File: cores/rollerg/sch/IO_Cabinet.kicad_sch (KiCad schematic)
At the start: 0 parts

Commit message: wip rollerg sch: SOUND
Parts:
- added C19, C20, C21, C23: 74LS253, symbol 74xx:74LS253
- added F14: 74LS04, symbol jt74:74LS04
- added RN1, RN2, RN3, RN4, RN5: KONAMI_005273, symbol konami:KONAMI_005273
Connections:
- new net: C23.3 (I3a), RN5.1 (YO)
- new net: C23.4 (I2a), RN5.3 (Y1)
- new net: C23.13 (I3b), RN5.5 (Y2)
- new net: C23.12 (I2b), RN5.7 (Y3)
- new net: C19.5 (I1a), RN2.1 (YO)
- new net: C19.11 (I1b), RN2.3 (Y1)
- new net: C20.5 (I1a), RN2.5 (Y2)
- new net: C20.11 (I1b), RN2.7 (Y3)
- new net: C20.3 (I3a), RN3.1 (YO)
- new net: C20.4 (I2a), RN3.3 (Y1)
- new net: C20.13 (I3b), RN3.5 (Y2)
- new net: C20.12 (I2b), RN3.7 (Y3)
- new net: C19.12 (I2b), RN1.7 (Y3)
- new net: C19.13 (I3b), RN1.5 (Y2)
- new net: C19.3 (I3a), RN1.1 (YO)
- new net: C19.4 (I2a), RN1.3 (Y1)
- new net: C21.3 (I3a), RN4.1 (YO)
- new net: C21.4 (I2a), RN4.3 (Y1)
- new net: C21.13 (I3b), RN4.5 (Y2)
- new net: C21.12 (I2b), RN4.7 (Y3)
- new net DB0: C21.9 (Zb)
- new net DB1: C21.7 (Za)
- new net DB2: C23.9 (Zb)
- new net DB3: C23.7 (Za)
- new net DB4: C20.9 (Zb)
- new net DB5: C20.7 (Za)
- new net DB6: C19.9 (Zb)
- new net DB7: C19.7 (Za)
- new net MAIN_A1: F14.1
- new net MOE: C19.1 (OEa), C19.15 (OEb), C20.1 (OEa), C20.15 (OEb), C21.1 (OEa), C21.15 (OEb), C23.1 (OEa), C23.15 (OEb)
- new net SMU: C19.14 (A0), C20.14 (A0), C21.14 (A0), C23.14 (A0)
- new net SMUB: C19.2 (A1), C20.2 (A1), C21.2 (A1), C23.2 (A1), F14.2
- new net VCC: C19.16 (VCC), C20.16 (VCC), C21.16 (VCC), C23.16 (VCC)
- new net VSS: C19.10 (I0b), C19.6 (I0a), C19.8 (GND), C20.10 (I0b), C20.6 (I0a), C20.8 (GND), C21.10 (I0b), C21.11 (I1b), C21.5 (I1a), C21.6 (I0a), C21.8 (GND), C23.10 (I0b), C23.11 (I1b), C23.5 (I1a), C23.6 (I0a), C23.8 (GND)

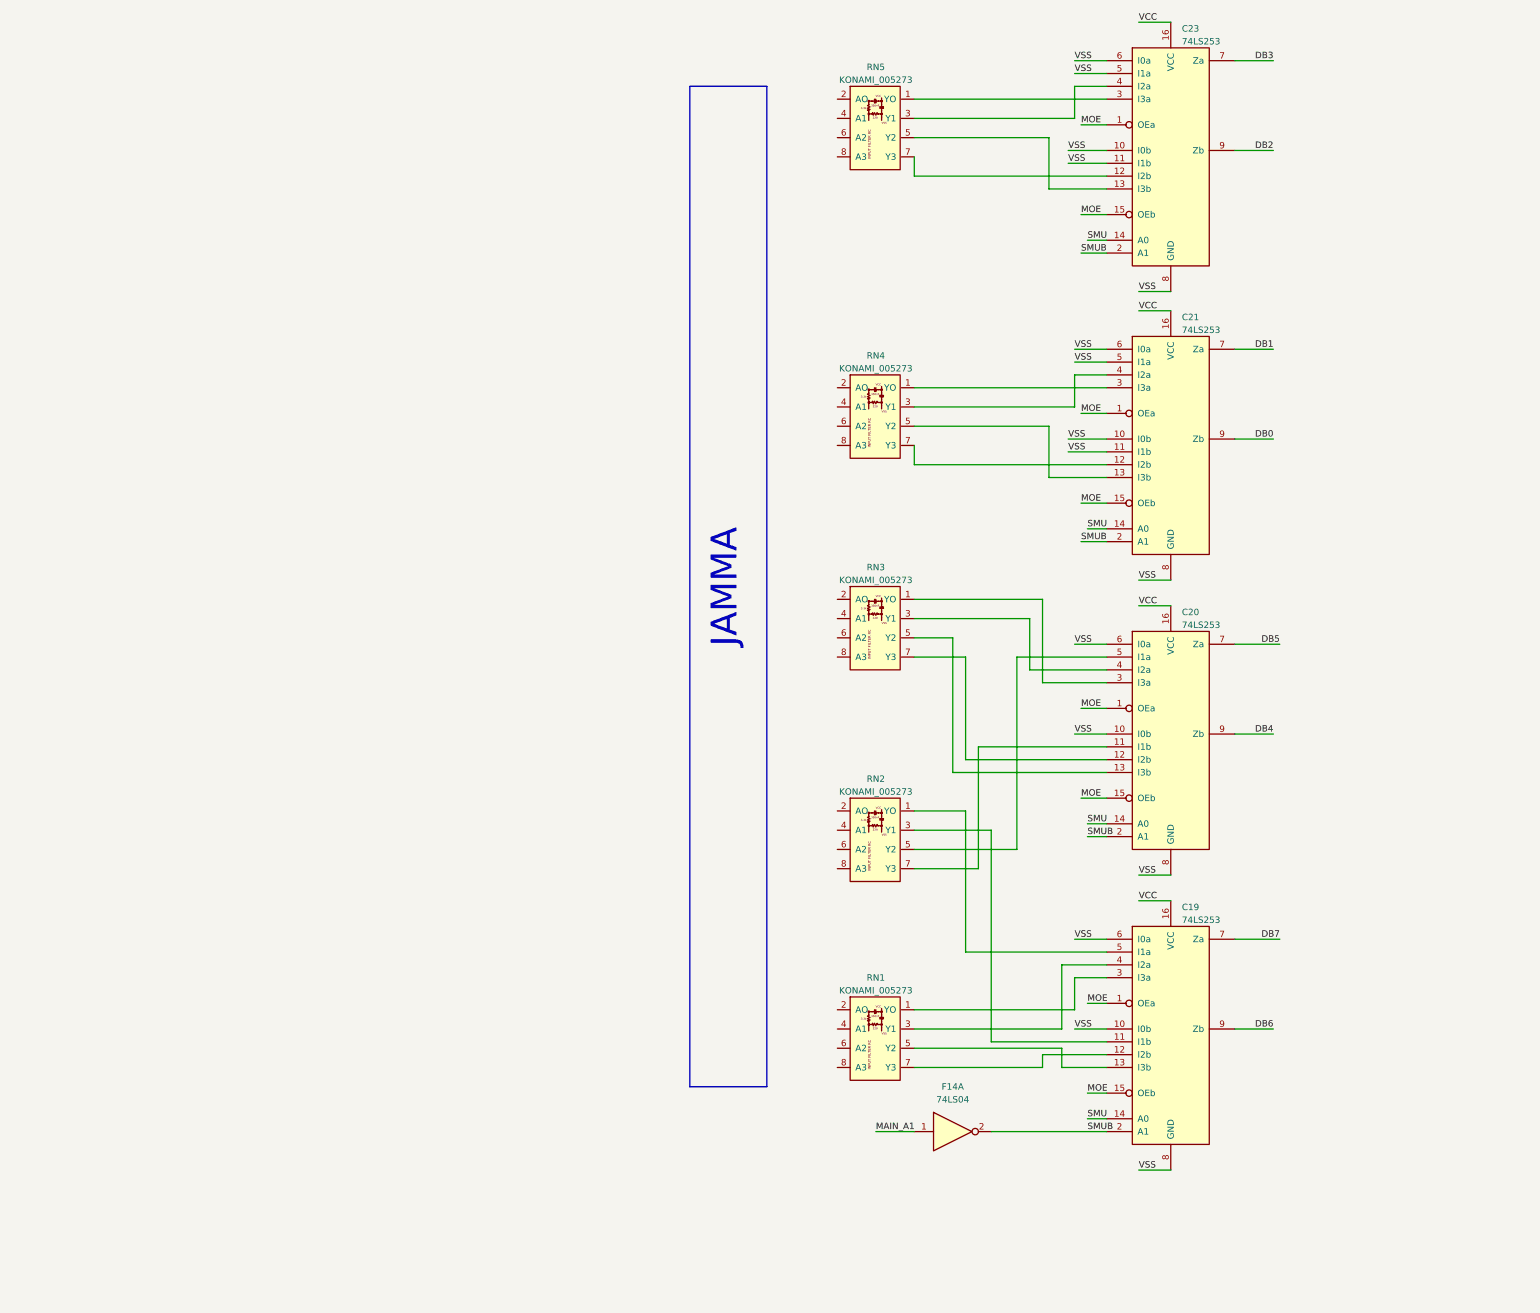
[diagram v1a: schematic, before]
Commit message: wip rollerg sch: CABINET AND RGB
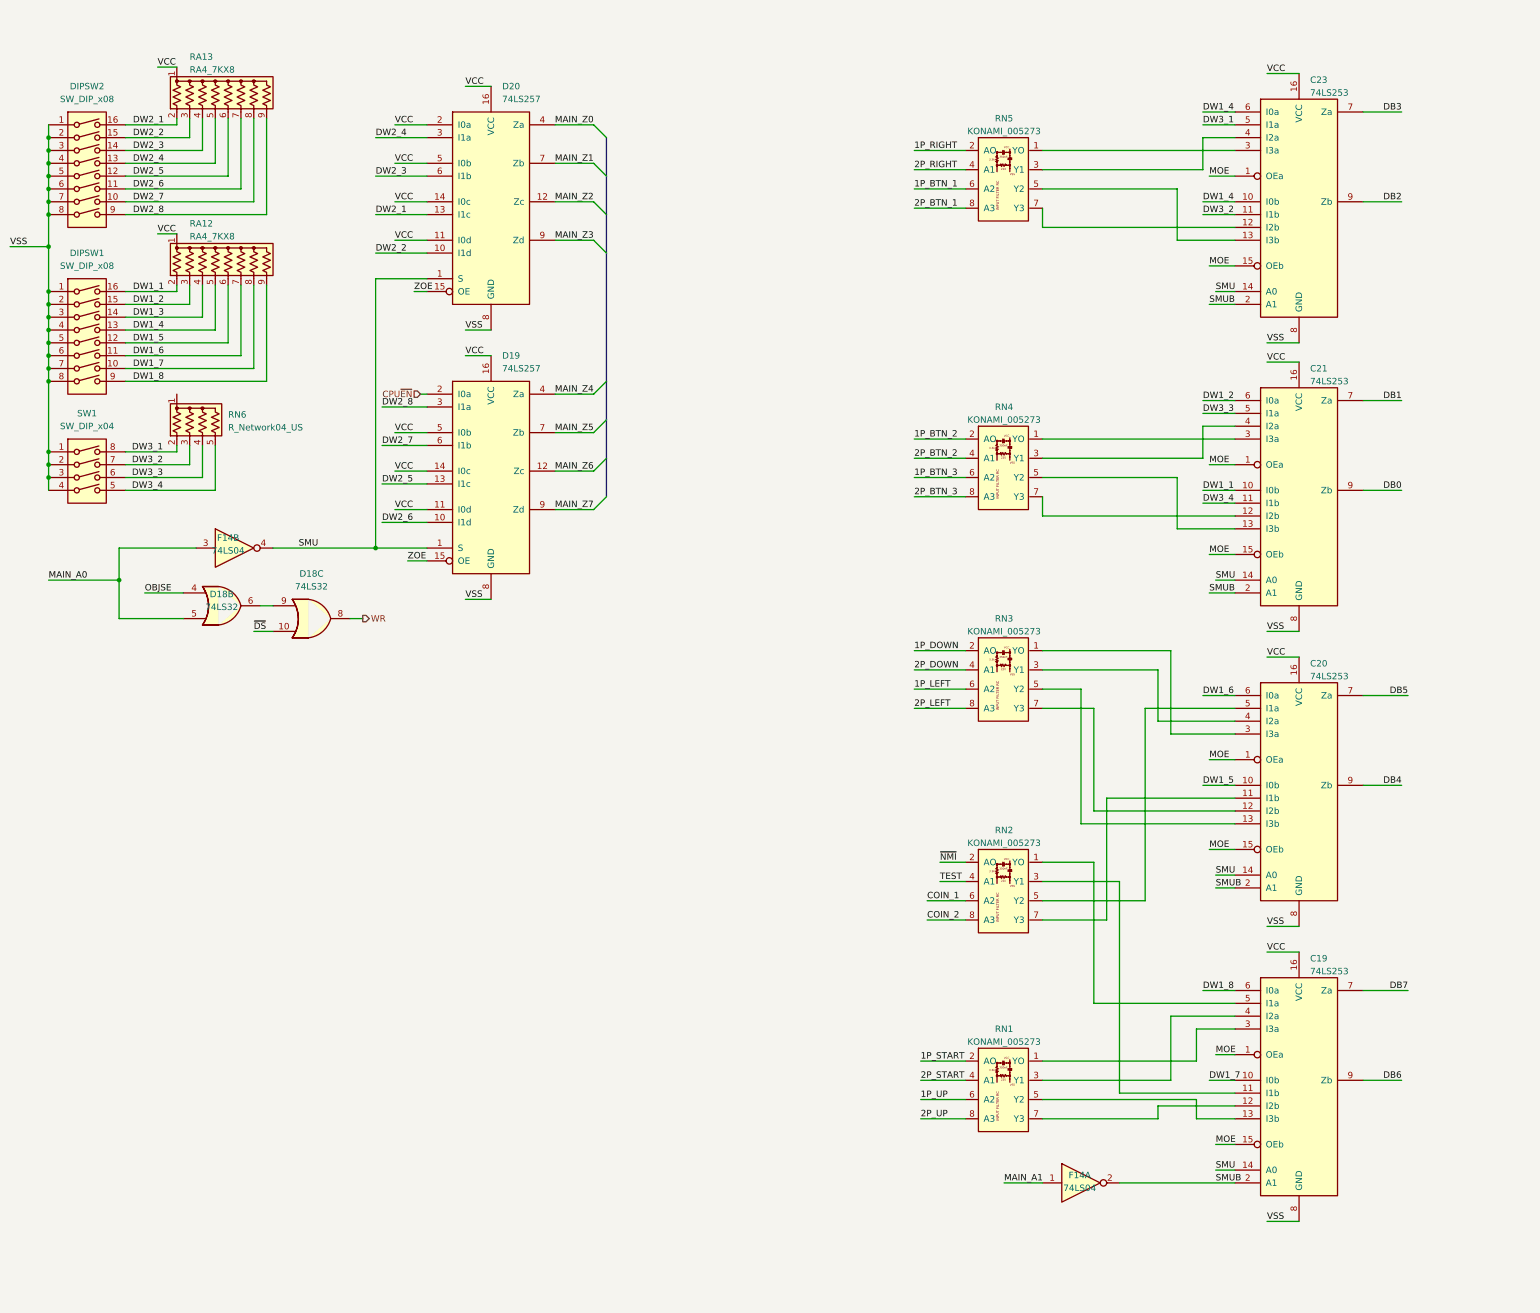
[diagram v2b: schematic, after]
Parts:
- added D18: 74LS32, symbol jt74:74LS32
- added D19, D20: 74LS257, symbol 74xx:74LS257
- added DIPSW1, DIPSW2: SW_DIP_x08, symbol Switch:SW_DIP_x08
- added unit 2 of F14
- added RA12, RA13: RA4_7KX8, Resistor_THT:R_Array_SIP7, symbol Device:R_Network08_US
- added RN6: R_Network04_US, Resistor_THT:R_Array_SIP5, symbol Device:R_Network04_US
- added SW1: SW_DIP_x04, symbol Switch:SW_DIP_x04
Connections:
- net SMU: now also D19.1 (S), D20.1 (S), F14.4
- net VCC: now also D19.11 (I0d), D19.14 (I0c), D19.16 (VCC), D19.5 (I0b), D20.11 (I0d), D20.14 (I0c), D20.16 (VCC), D20.2 (I0a), D20.5 (I0b), RA12.1 (common), RA13.1 (common)
- net VSS: now also D19.8 (GND), D20.8 (GND), DIPSW1.1, DIPSW1.2, DIPSW1.3, DIPSW1.4, DIPSW1.5, DIPSW1.6, DIPSW1.7, DIPSW1.8, DIPSW2.1, DIPSW2.2, DIPSW2.3, DIPSW2.4, DIPSW2.5, DIPSW2.6, DIPSW2.7, DIPSW2.8, SW1.1, SW1.2, SW1.3, SW1.4; no longer C19.10 (I0b), C19.6 (I0a), C20.10 (I0b), C20.6 (I0a), C21.10 (I0b), C21.11 (I1b), C21.5 (I1a), C21.6 (I0a), C23.10 (I0b), C23.11 (I1b), C23.5 (I1a), C23.6 (I0a)
- net 1P_RIGHT: now reaches RN5.2 (AO)
- net 2P_RIGHT: now reaches RN5.4 (A1)
- net 1P_BTN_1: now reaches RN5.6 (A2)
- net 2P_BTN_1: now reaches RN5.8 (A3)
- net ~{NMI}: now reaches RN2.2 (AO)
- net TEST: now reaches RN2.4 (A1)
- net COIN_1: now reaches RN2.6 (A2)
- net COIN_2: now reaches RN2.8 (A3)
- net 1P_DOWN: now reaches RN3.2 (AO)
- net 2P_DOWN: now reaches RN3.4 (A1)
- net 1P_LEFT: now reaches RN3.6 (A2)
- net 2P_LEFT: now reaches RN3.8 (A3)
- net 1P_BTN_2: now reaches RN4.2 (AO)
- net 2P_BTN_2: now reaches RN4.4 (A1)
- net 1P_BTN_3: now reaches RN4.6 (A2)
- net 2P_BTN_3: now reaches RN4.8 (A3)
- net 1P_START: now reaches RN1.2 (AO)
- net 2P_START: now reaches RN1.4 (A1)
- net 1P_UP: now reaches RN1.6 (A2)
- net 2P_UP: now reaches RN1.8 (A3)
- new net: D18.6, D18.9
- new net CPU~{EN}: D19.2 (I0a)
- new net DW1_1: C21.10 (I0b), DIPSW1.16, RA12.2 (R1)
- new net DW1_2: C21.6 (I0a), DIPSW1.15, RA12.3 (R2)
- new net DW1_3: DIPSW1.14, RA12.4 (R3)
- new net DW1_4: C23.10 (I0b), C23.6 (I0a), DIPSW1.13, RA12.5 (R4)
- new net DW1_5: C20.10 (I0b), DIPSW1.12, RA12.6 (R5)
- new net DW1_6: C20.6 (I0a), DIPSW1.11, RA12.7 (R6)
- new net DW1_7: C19.10 (I0b), DIPSW1.10, RA12.8 (R7)
- new net DW1_8: C19.6 (I0a), DIPSW1.9, RA12.9 (R8)
- new net DW2_1: D20.13 (I1c), DIPSW2.16, RA13.2 (R1)
- new net DW2_2: D20.10 (I1d), DIPSW2.15, RA13.3 (R2)
- new net DW2_3: D20.6 (I1b), DIPSW2.14, RA13.4 (R3)
- new net DW2_4: D20.3 (I1a), DIPSW2.13, RA13.5 (R4)
- new net DW2_5: D19.13 (I1c), DIPSW2.12, RA13.6 (R5)
- new net DW2_6: D19.10 (I1d), DIPSW2.11, RA13.7 (R6)
- new net DW2_7: D19.6 (I1b), DIPSW2.10, RA13.8 (R7)
- new net DW2_8: D19.3 (I1a), DIPSW2.9, RA13.9 (R8)
- new net DW3_1: C23.5 (I1a), RN6.2 (R1), SW1.8
- new net DW3_2: C23.11 (I1b), RN6.3 (R2), SW1.7
- new net DW3_3: C21.5 (I1a), RN6.4 (R3), SW1.6
- new net DW3_4: C21.11 (I1b), RN6.5 (R4), SW1.5
- new net MAIN_A0: D18.5, F14.3
- new net MAIN_Z0: D20.4 (Za)
- new net MAIN_Z1: D20.7 (Zb)
- new net MAIN_Z2: D20.12 (Zc)
- new net MAIN_Z3: D20.9 (Zd)
- new net MAIN_Z4: D19.4 (Za)
- new net MAIN_Z5: D19.7 (Zb)
- new net MAIN_Z6: D19.12 (Zc)
- new net MAIN_Z7: D19.9 (Zd)
- new net OBJSE: D18.4
- new net WR: D18.8
- new net ZOE: D19.15 (OE), D20.15 (OE)
- new net ~{DS}: D18.10
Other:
- moved on the sheet: C19, C20, C21, C23, F14A, RN1, RN2, RN3, RN4, RN5

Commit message: almost complete rollerg sch
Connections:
- net MAIN_Z0 is gone; now on net DB7: D20.4 (Za)
- net MAIN_Z1 is gone; now on net DB6: D20.7 (Zb)
- net MAIN_Z2 is gone; now on net DB5: D20.12 (Zc)
- net MAIN_Z3 is gone; now on net DB4: D20.9 (Zd)
- net MAIN_Z4 is gone; now on net DB3: D19.4 (Za)
- net MAIN_Z5 is gone; now on net DB2: D19.7 (Zb)
- net MAIN_Z6 is gone; now on net DB1: D19.12 (Zc)
- net MAIN_Z7 is gone; now on net DB0: D19.9 (Zd)
- net VCC: now also RN6.1 (common)
- net OBCE: now reaches D18.6, D18.9
- net VSS renamed GNDPWR
